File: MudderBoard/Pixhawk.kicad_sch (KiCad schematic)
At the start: 18 parts, among them U1 TPS566242DRLR, U2 LP38691DTX-3.3/NOPB

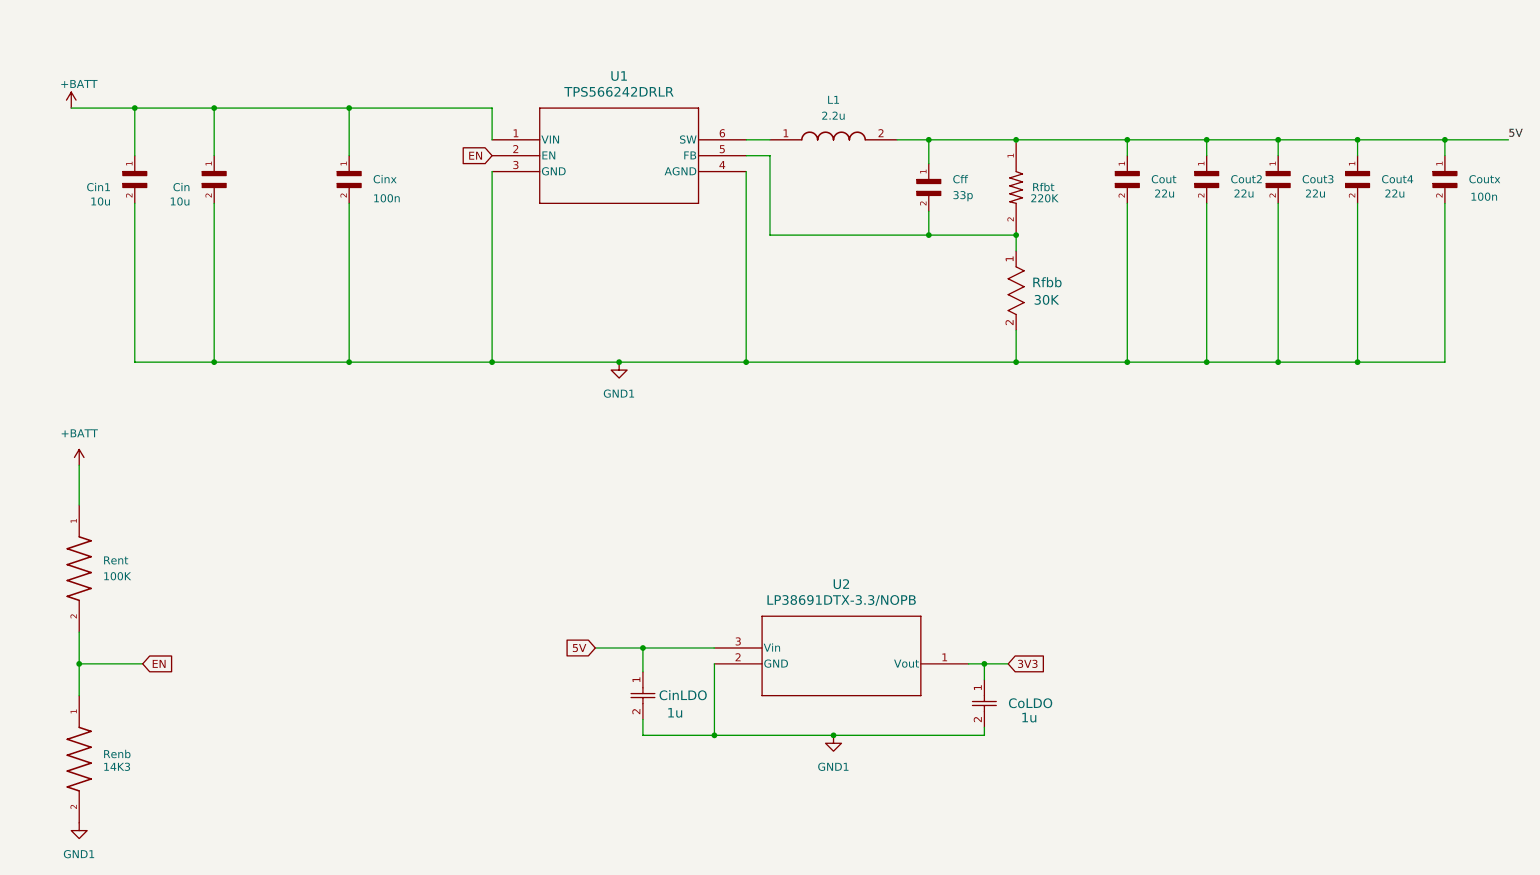
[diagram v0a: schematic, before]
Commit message: Layout
Pixhawk and Lidar
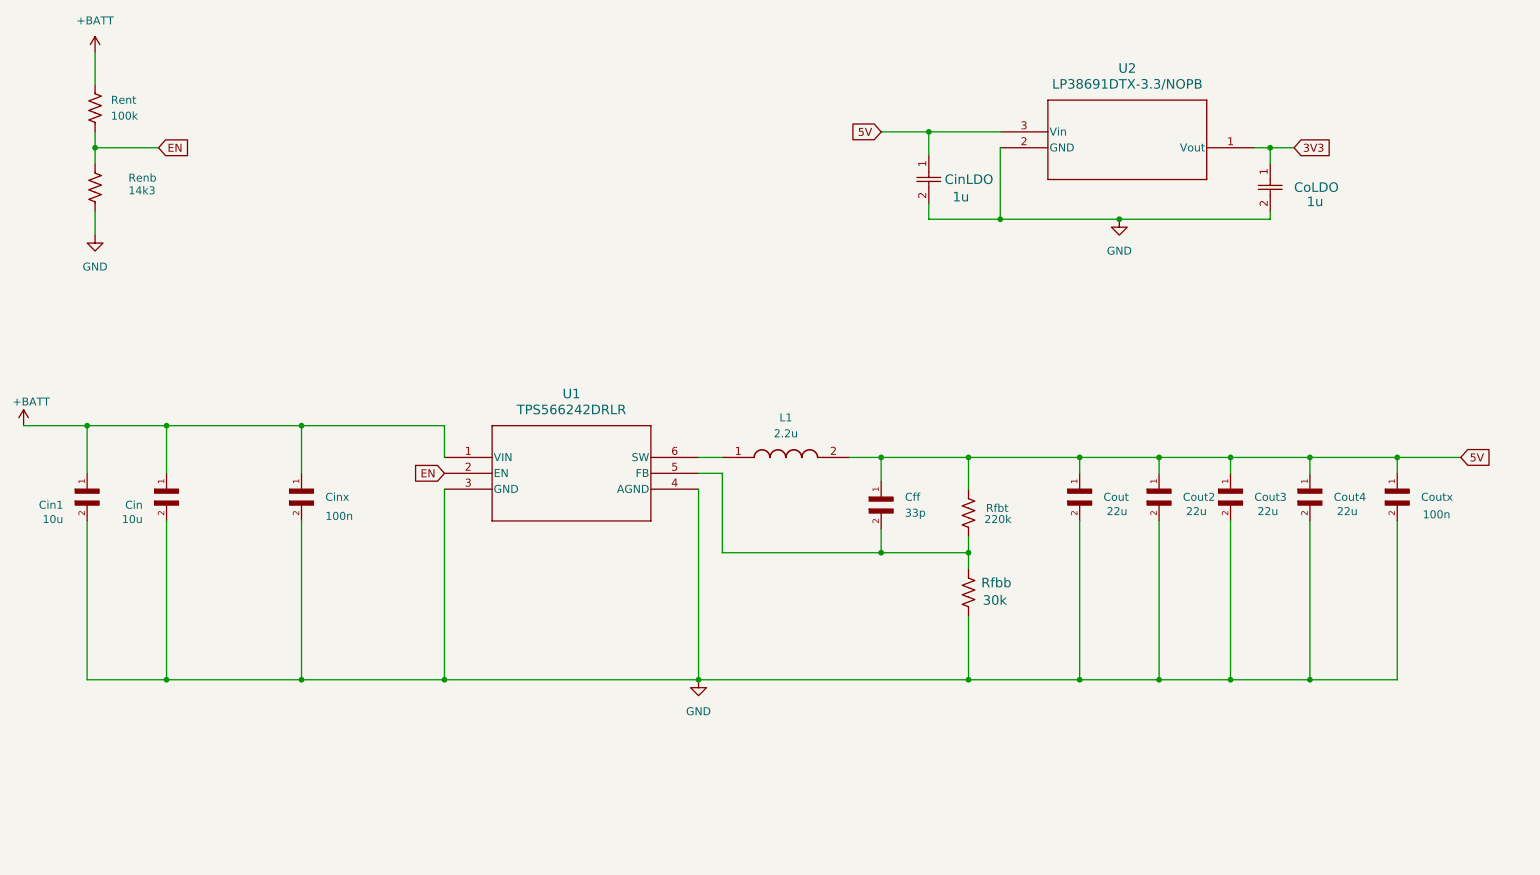
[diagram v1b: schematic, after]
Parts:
- Renb: value 14K3 -> 14k3; symbol R1:CRCW040214K3FKED -> Device:R_US
- Rent: value 100K -> 100k; footprint PH_Foot:RESC1005X40N -> Resistor_SMD:R_0402_1005Metric_Pad0.72x0.64mm_HandSolder; symbol R2:CRCW0402100KFKED -> Device:R_US
- Rfbb: value 30K -> 30k; footprint PH_Foot:R0603 -> Resistor_SMD:R_0603_1608Metric_Pad0.98x0.95mm_HandSolder; symbol Rfb2:RC0603FR-0730KL -> Device:R_US
- Rfbt: value 220K -> 220k; footprint PH_Foot:RESC1607X60N -> Resistor_SMD:R_0603_1608Metric_Pad0.98x0.95mm_HandSolder; symbol Rfb1:RC0603FR-07220KL -> Device:R_US
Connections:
- net GND1 renamed GND
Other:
- moved on the sheet: Cff, Cin, Cin1, CinLDO, Cinx, CoLDO, Cout, Cout2, Cout3, Cout4, Coutx, L1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

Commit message: Schematic updates
global labels and test points
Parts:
- added TP33, TP34, TP35, TP36, TP37, TP38: TestPoint, TestPoint:TestPoint_Pad_1.0x1.0mm, symbol Connector:TestPoint
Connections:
- net +BATT: now also TP33.1
- net 3V3: now also TP37.1
- net 5V: now also TP34.1, TP36.1
- net EN: now also TP38.1
- net at Cff.2, Rfbb.1, Rfbt.2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: now also TP35.1

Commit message: Schematic and Layout
TPs and net labels
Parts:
- removed TP34: TestPoint, TestPoint:TestPoint_Pad_1.0x1.0mm, symbol Connector:TestPoint
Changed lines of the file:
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@@
-	)
-	(junction
-		(at 255.27 95.25)
-		(diameter 0)
-		(color 0 0 0 0)
 	)
 	(junction
@@
 	(wire
 		(pts
-			(xy 255.27 95.25) (xy 261.62 95.25)
+			(xy 251.46 95.25) (xy 261.62 95.25)
 		)
 		(stroke
@@
 		(pts
 			(xy 237.49 130.81) (xy 251.46 130.81)
-		)
-		(stroke
-			(width 0)
-			(type default)
-		)
-	)
-	(wire
-		(pts
-			(xy 251.46 95.25) (xy 255.27 95.25)
 		)
 		(stroke
@@
 			)
 		)
-	)
-	(symbol
-		(lib_id "Connector:TestPoint")
-		(at 255.27 95.25 0)
-		(unit 1)
-		(exclude_from_sim no)
-		(in_bom yes)
-		(on_board yes)
-		(dnp no)
-		(fields_autoplaced yes)
-		(property "Reference" "TP34"
-			(at 257.81 90.6779 0)
-			(effects
-				(font
-					(size 1.27 1.27)
-				)
-				(justify left)
-			)
-		)
-		(property "Value" "TestPoint"
-			(at 257.81 93.2179 0)
-			(effects
-				(font
-					(size 1.27 1.27)
-				)
-				(justify left)
-			)
-		)
-		(property "Footprint" "TestPoint:TestPoint_Pad_1.0x1.0mm"
-			(at 260.35 95.25 0)
-			(effects
-				(font
-					(size 1.27 1.27)
-				)
-				(hide yes)
-			)
-		)
-		(property "Datasheet" "~"
-			(at 260.35 95.25 0)
-			(effects
-				(font
-					(size 1.27 1.27)
-				)
-				(hide yes)
-			)
-		)
-		(property "Description" "test point"
-			(at 255.27 95.25 0)
-			(effects
-				(font
-					(size 1.27 1.27)
-				)
-				(hide yes)
-			)
-		)
-		(pin "1"
-		)
-		(instances
-			(project "MudderBoard"
-				(path "/cdf98bf7-80ce-4b13-b655-e6c7c589c122/0627c6a6-a63c-4c7b-88fc-6e03d8d4f91c"
-					(reference "TP34")
-					(unit 1)
-				)
-			)
-		)
